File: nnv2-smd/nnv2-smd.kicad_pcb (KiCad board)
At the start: 2 copper layers, 52.6 x 27.9 mm, 4 parts, among them J1 Conn_01x02_Socket, J2 Conn_01x04_Socket, SW1 SW_SPST, U1 Nice! Nano (ProMicro)

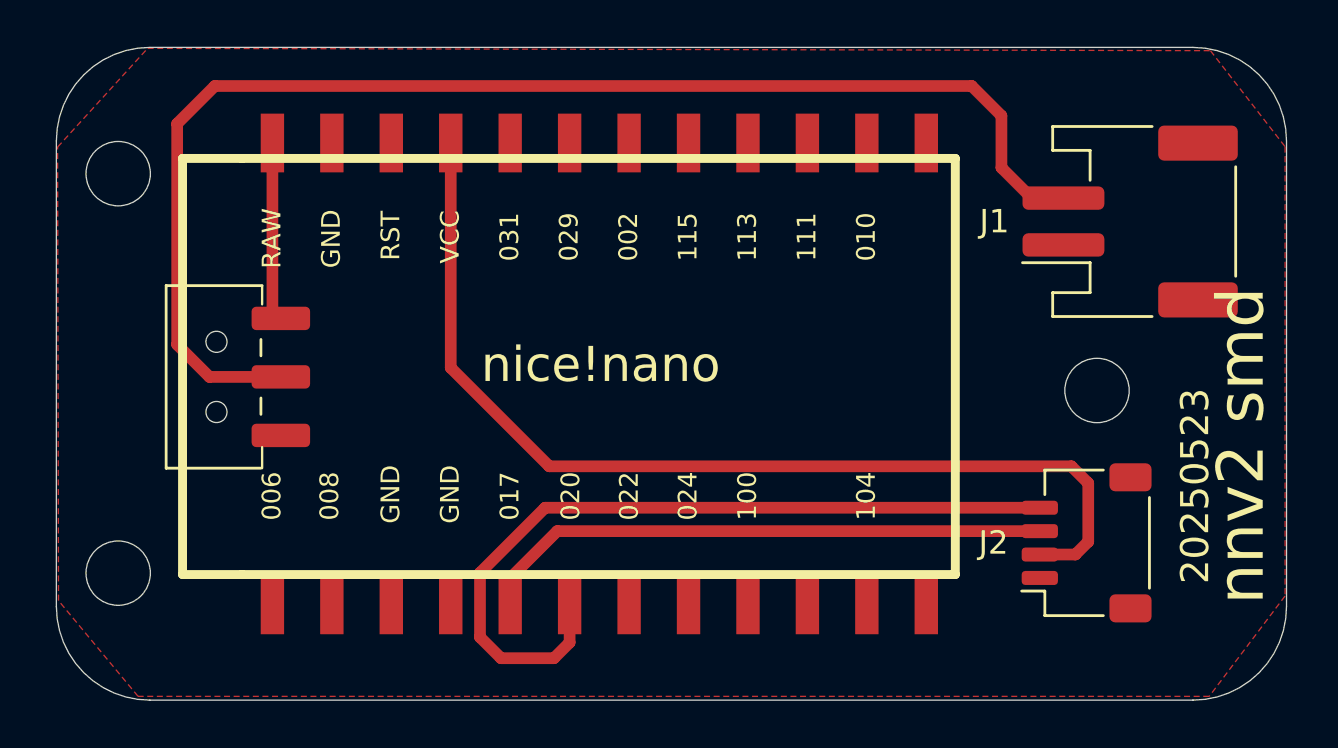
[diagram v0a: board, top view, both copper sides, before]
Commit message: cad step case
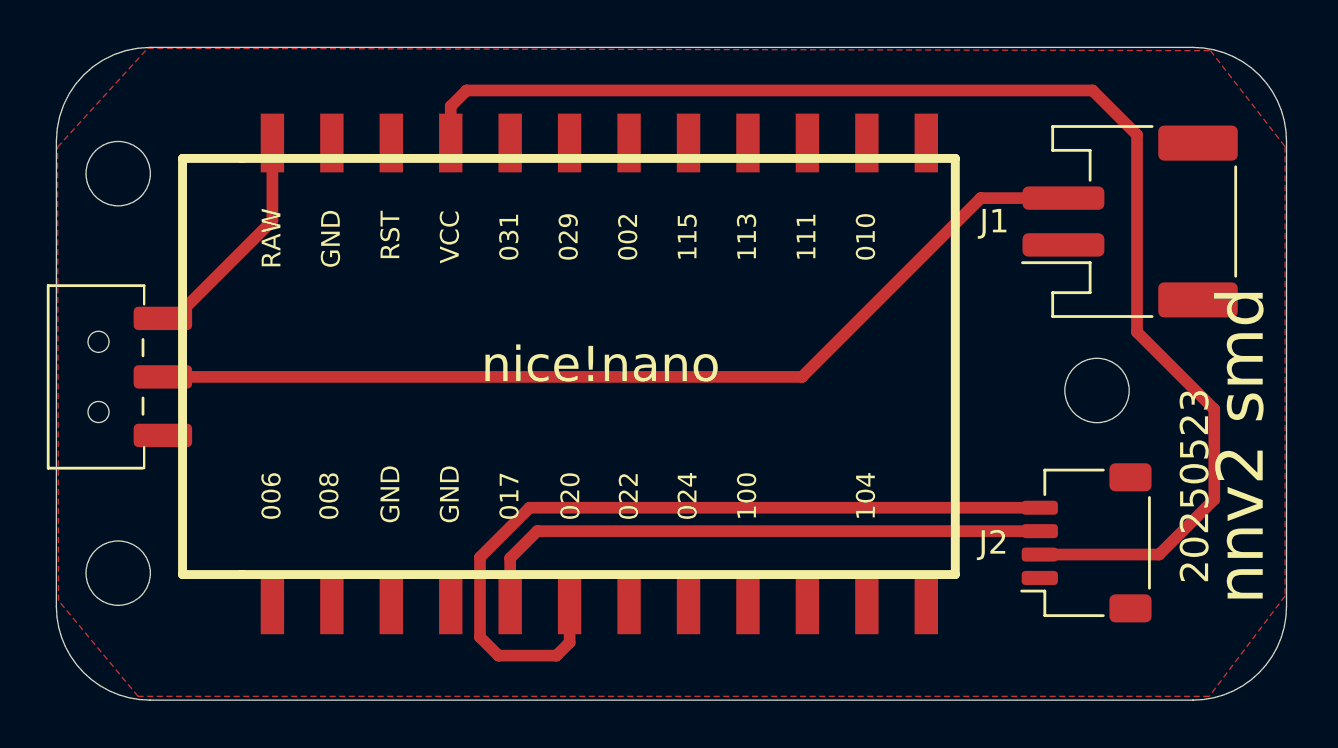
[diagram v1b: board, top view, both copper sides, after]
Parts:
- moved SW1 5.04 mm to (166.6, 88.4)
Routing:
- net /rawswitch: track 56.3 -> 41.1 mm
- net VCC: track 43.7 -> 57.3 mm
- net /RAW: track 7.64 -> 9.23 mm
- net /SDA: track 24.6 -> 25.1 mm
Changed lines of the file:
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@@
 			(pdf_single_document no)
 			(dxfpolygonmode yes)
-			(dxfimperialunits yes)
+			(dxfimperialunits no)
 			(dxfusepcbnewfont yes)
 			(psnegative no)
@@
 			(crossoutdnponfab yes)
 			(subtractmaskfromsilk no)
-			(outputformat 1)
+			(outputformat 3)
 			(mirror no)
-			(drillshape 1)
+			(drillshape 0)
 			(scaleselection 1)
 			(outputdirectory "")
@@
 	(footprint "footprints:slide-switch-smd"
 		(layer "F.Cu")
-		(at 171.59 88.44 -90)
+		(at 166.55 88.44 -90)
 		(property "Reference" "SW1"
 			(at 0 -0.5 270)
@@
 		)
 		(embedded_fonts no)
-		(model "/Users/sklarm/Documents/KiCad/mikeysklar/3dmodels/slide-switch-smt-mskt-12c03-Part.step"
+		(model "/Users/sklarm/Documents/KiCad/mikeysklar/3dmodels/slide-switch-mskt-12c03.step"
 			(offset
-				(xyz 3.5 3 0)
+				(xyz -0.1 0 0)
 			)
 			(scale
@@
 			)
 			(rotate
-				(xyz -180 -180 -0)
+				(xyz -0 -0 -180)
 			)
 		)
@@
 	)
 	(gr_line
-		(start 164.498427 98.2516)
-		(end 164.498427 78.36)
+		(start 164.498428 98.251573)
+		(end 164.500001 78.35)
 		(stroke
 			(width 0.05)
@@
 	(gr_line
 		(start 213.061573 102.251573)
-		(end 168.498427 102.251573)
+		(end 168.498427 102.251571)
 		(stroke
 			(width 0.05)
@@
 	(gr_arc
 		(start 213.061573 74.36)
-		(mid 215.89 75.531573)
-		(end 217.061573 78.36)
+		(mid 215.895209 75.536764)
+		(end 217.061573 78.374696)
 		(stroke
 			(width 0.05)
@@
 	)
 	(gr_arc
-		(start 168.498427 102.251573)
-		(mid 165.67 101.08)
-		(end 164.498427 98.251573)
+		(start 168.498427 102.251572)
+		(mid 165.669993 101.080007)
+		(end 164.498428 98.251573)
+		(stroke
+			(width 0.05)
+			(type solid)
+		)
+		(layer "Edge.Cuts")
+	)
+	(gr_arc
+		(start 217.061572 98.251573)
+		(mid 215.890007 101.080007)
+		(end 213.061573 102.251572)
 		(stroke
 			(width 0.05)
@@
 	)
 	(gr_arc
-		(start 217.061573 98.251573)
-		(mid 215.89 101.08)
-		(end 213.061573 102.251573)
+		(start 164.5 78.35)
+		(mid 165.674643 75.529153)
+		(end 168.498427 74.361587)
 		(stroke
 			(width 0.05)
-			(type default)
-		)
-		(layer "Edge.Cuts")
-	)
-	(gr_arc
-		(start 164.498427 78.36)
-		(mid 165.67 75.531573)
-		(end 168.498427 74.36)
-		(stroke
-			(width 0.05)
-			(type default)
+			(type solid)
 		)
 		(layer "Edge.Cuts")
@@
 	(gr_line
 		(start 168.498427 74.36)
-		(end 213.061573 74.36)
+		(end 213.0616 74.36)
 		(stroke
 			(width 0.05)
@@
 	)
 	(segment
-		(start 174.09 88.44)
-		(end 171.04 88.44)
+		(start 196.36 88.44)
+		(end 204 80.8)
 		(width 0.5)
 		(layer "F.Cu")
@@
 	)
 	(segment
-		(start 171.27 76.01)
-		(end 203.61 76.01)
+		(start 169.55 88.44)
+		(end 196.36 88.44)
 		(width 0.5)
 		(layer "F.Cu")
@@
 	)
 	(segment
-		(start 204.88 77.28)
-		(end 204.88 79.5)
-		(width 0.5)
-		(layer "F.Cu")
-		(net 1)
-	)
-	(segment
-		(start 204.88 79.5)
-		(end 206.18 80.8)
-		(width 0.5)
-		(layer "F.Cu")
-		(net 1)
-	)
-	(segment
-		(start 169.66 77.62)
-		(end 171.27 76.01)
-		(width 0.5)
-		(layer "F.Cu")
-		(net 1)
-	)
-	(segment
-		(start 171.04 88.44)
-		(end 169.66 87.06)
-		(width 0.5)
-		(layer "F.Cu")
-		(net 1)
-	)
-	(segment
-		(start 169.66 87.06)
-		(end 169.66 77.62)
-		(width 0.5)
-		(layer "F.Cu")
-		(net 1)
-	)
-	(segment
-		(start 206.18 80.8)
+		(start 204 80.8)
 		(end 207.53 80.8)
 		(width 0.5)
@@
 	)
 	(segment
-		(start 203.61 76.01)
-		(end 204.88 77.28)
-		(width 0.5)
-		(layer "F.Cu")
-		(net 1)
-	)
-	(segment
-		(start 183.89 97.04)
-		(end 185.9 95.03)
+		(start 183.89 96.185)
+		(end 185.045 95.03)
 		(width 0.5)
 		(layer "F.Cu")
@@
 	(segment
 		(start 183.89 98.18)
-		(end 183.89 97.04)
+		(end 183.89 96.185)
 		(width 0.5)
 		(layer "F.Cu")
@@
 	)
 	(segment
-		(start 185.9 95.03)
+		(start 185.045 95.03)
 		(end 206.52 95.03)
 		(width 0.5)
@@
 	)
 	(segment
-		(start 208.59 92.98)
-		(end 208.59 95.48)
+		(start 213.975 93.675)
+		(end 211.62 96.03)
 		(width 0.5)
 		(layer "F.Cu")
@@
 	)
 	(segment
-		(start 208.04 96.03)
+		(start 213.975 89.825)
+		(end 213.975 93.675)
+		(width 0.5)
+		(layer "F.Cu")
+		(net 4)
+	)
+	(segment
+		(start 211.62 96.03)
 		(end 206.52 96.03)
 		(width 0.5)
@@
 	)
 	(segment
-		(start 181.35 88.05)
-		(end 185.56 92.26)
+		(start 181.35 78.445)
+		(end 181.35 76.875)
 		(width 0.5)
 		(layer "F.Cu")
@@
 	)
 	(segment
-		(start 181.35 78.445)
-		(end 181.35 88.05)
+		(start 208.775 76.2)
+		(end 210.675 78.1)
 		(width 0.5)
 		(layer "F.Cu")
@@
 	)
 	(segment
-		(start 208.59 95.48)
-		(end 208.04 96.03)
+		(start 181.35 76.875)
+		(end 182.025 76.2)
 		(width 0.5)
 		(layer "F.Cu")
@@
 	)
 	(segment
-		(start 207.87 92.26)
-		(end 208.59 92.98)
+		(start 210.675 86.525)
+		(end 213.975 89.825)
 		(width 0.5)
 		(layer "F.Cu")
@@
 	)
 	(segment
-		(start 185.56 92.26)
-		(end 207.87 92.26)
+		(start 182.025 76.2)
+		(end 208.775 76.2)
 		(width 0.5)
 		(layer "F.Cu")
@@
 	)
 	(segment
-		(start 183.5 100.46)
+		(start 210.675 78.1)
+		(end 210.675 86.525)
+		(width 0.5)
+		(layer "F.Cu")
+		(net 4)
+	)
+	(segment
+		(start 184.72 94.03)
+		(end 206.52 94.03)
+		(width 0.5)
+		(layer "F.Cu")
+		(net 5)
+	)
+	(segment
+		(start 186.43 99.79)
+		(end 185.87 100.35)
+		(width 0.5)
+		(layer "F.Cu")
+		(net 5)
+	)
+	(segment
+		(start 182.6 96.15)
+		(end 184.72 94.03)
+		(width 0.5)
+		(layer "F.Cu")
+		(net 5)
+	)
+	(segment
+		(start 182.6 99.56)
+		(end 182.6 96.15)
+		(width 0.5)
+		(layer "F.Cu")
+		(net 5)
+	)
+	(segment
+		(start 183.39 100.35)
 		(end 182.6 99.56)
 		(width 0.5)
@@
 	)
 	(segment
-		(start 185.76 100.46)
-		(end 183.5 100.46)
+		(start 185.87 100.35)
+		(end 183.39 100.35)
 		(width 0.5)
 		(layer "F.Cu")
@@
 	)
 	(segment
-		(start 186.43 99.79)
-		(end 185.76 100.46)
-		(width 0.5)
-		(layer "F.Cu")
-		(net 5)
-	)
-	(segment
-		(start 182.6 96.813)
-		(end 185.383 94.03)
-		(width 0.5)
-		(layer "F.Cu")
-		(net 5)
-	)
-	(segment
-		(start 185.383 94.03)
-		(end 206.52 94.03)
-		(width 0.5)
-		(layer "F.Cu")
-		(net 5)
-	)
-	(segment
-		(start 182.6 99.56)
-		(end 182.6 96.813)
-		(width 0.5)
-		(layer "F.Cu")
-		(net 5)
-	)
-	(segment
-		(start 173.73 85.58)
-		(end 174.09 85.94)
+		(start 169.55 85.94)
+		(end 173.73 81.76)
 		(width 0.5)
 		(layer "F.Cu")
@@
 	)
 	(segment
-		(start 173.73 78.445)
-		(end 173.73 85.58)
+		(start 173.73 81.76)
+		(end 173.73 78.445)
 		(width 0.5)
 		(layer "F.Cu")
